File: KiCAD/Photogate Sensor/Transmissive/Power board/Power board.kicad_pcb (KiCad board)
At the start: 2 copper layers, 35 x 35 mm, 7 parts, among them J1 USB_B_Micro, J2 FFC Socket, J3 Conn_01x03_Socket, J4 DC Jack

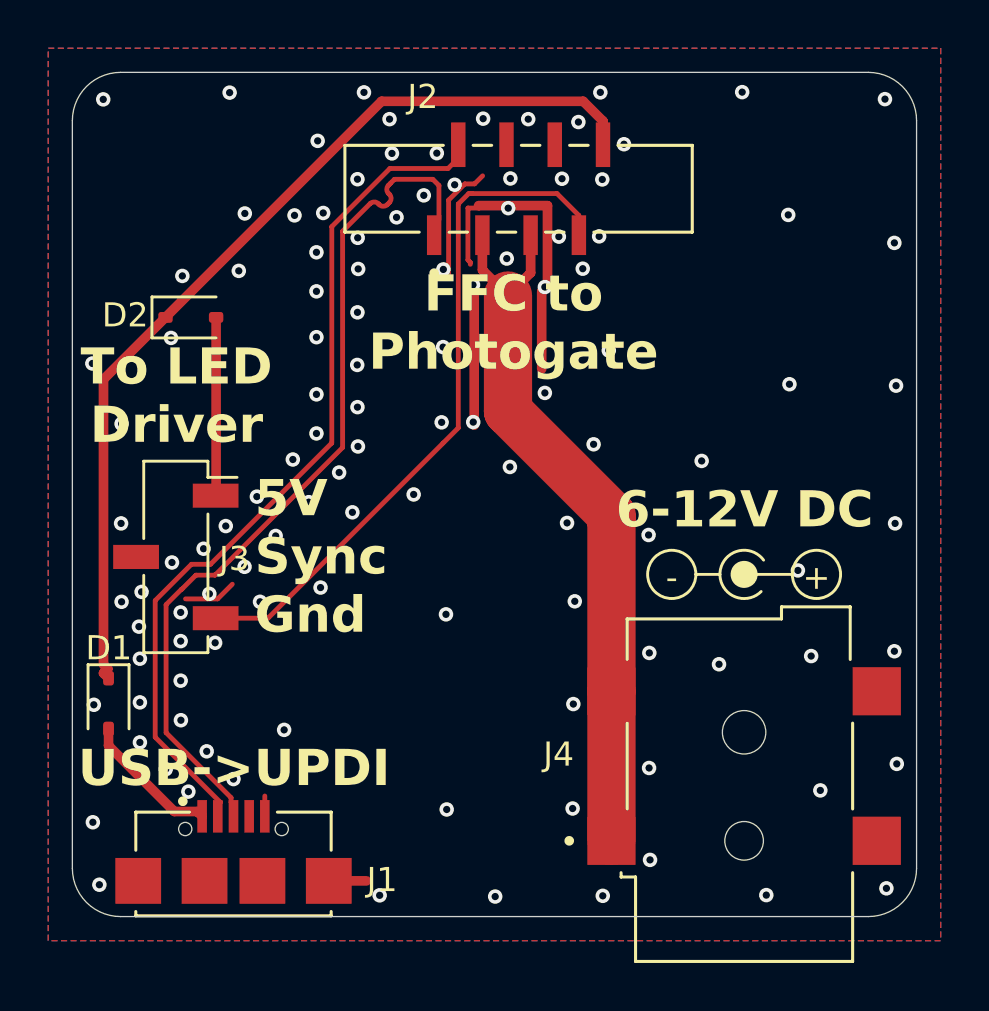
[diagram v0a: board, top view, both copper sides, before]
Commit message: USB skew matched and impedance set to approx. 90 ohms
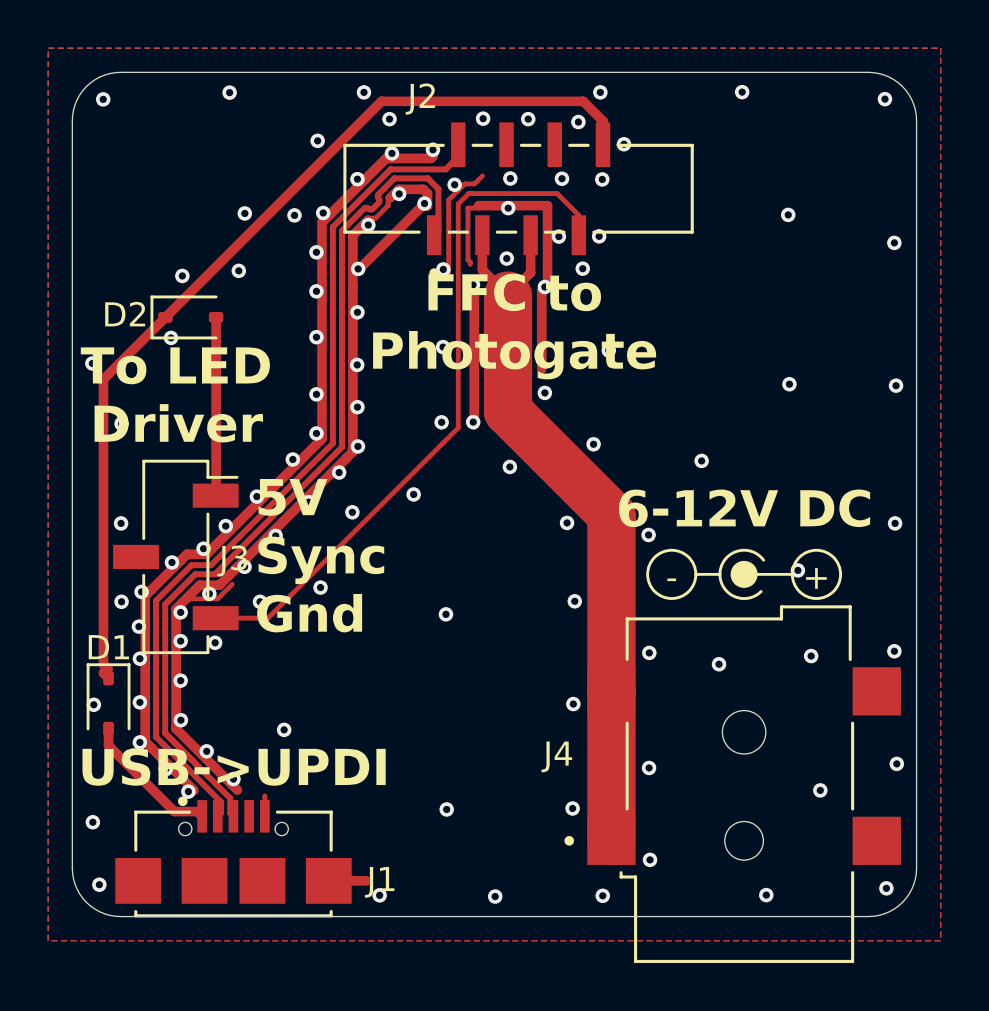
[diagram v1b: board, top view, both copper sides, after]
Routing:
- net GND: track 28.3 -> 98.7 mm
- net /D-: track 36.1 -> 37.6 mm
- net /D+: track 36.6 -> 37.8 mm

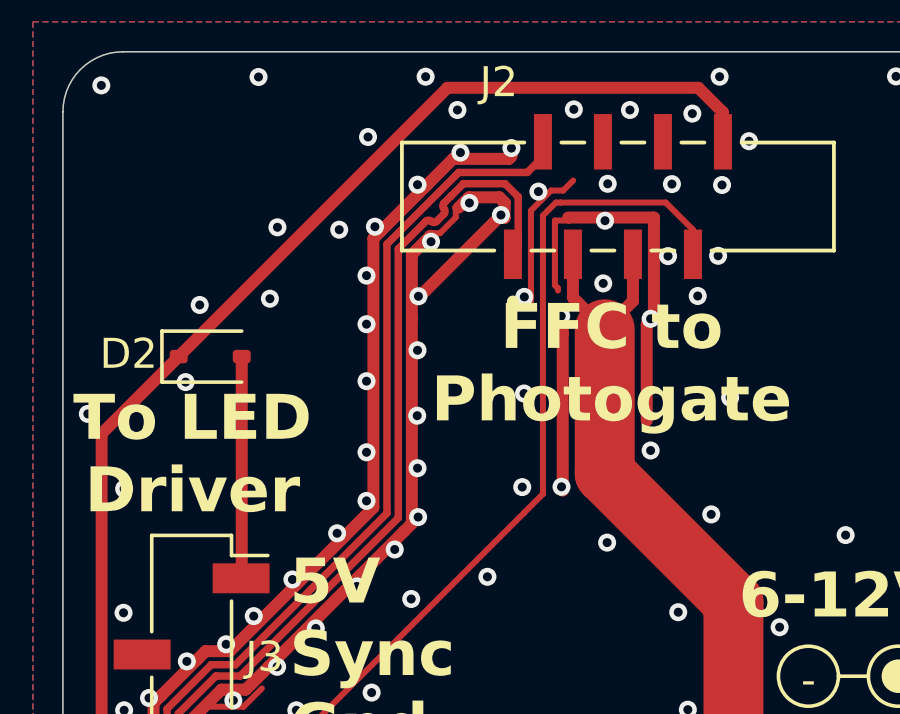
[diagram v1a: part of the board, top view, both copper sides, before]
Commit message: Add skew on power board D+ to offset skew on photogate board
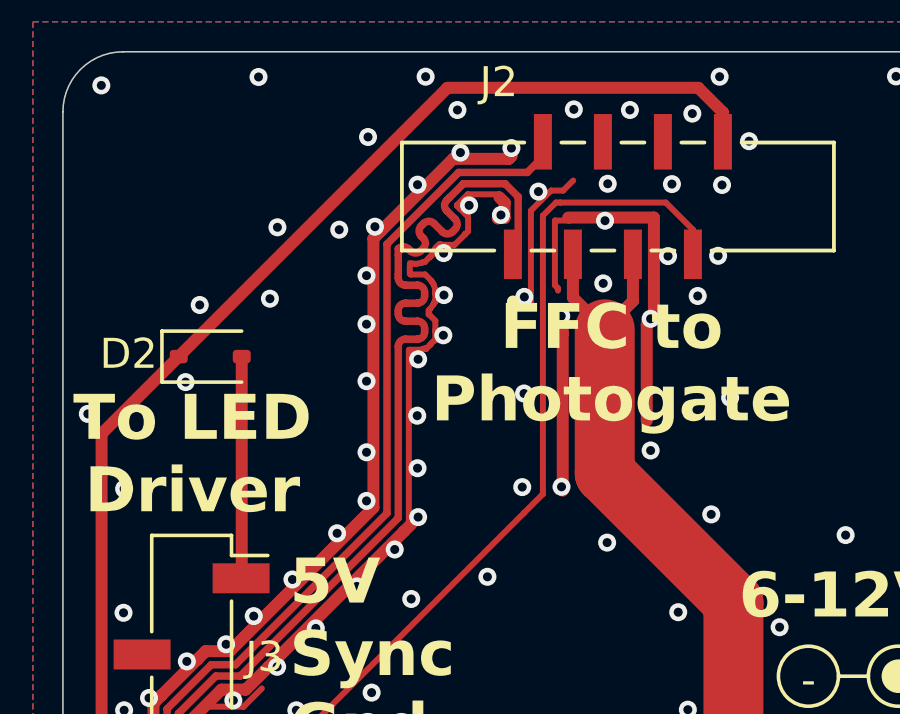
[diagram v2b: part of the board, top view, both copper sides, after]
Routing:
- net /D+: track 37.8 -> 42.2 mm
- net GND: track 98.7 -> 97.7 mm, vias 116 -> 117

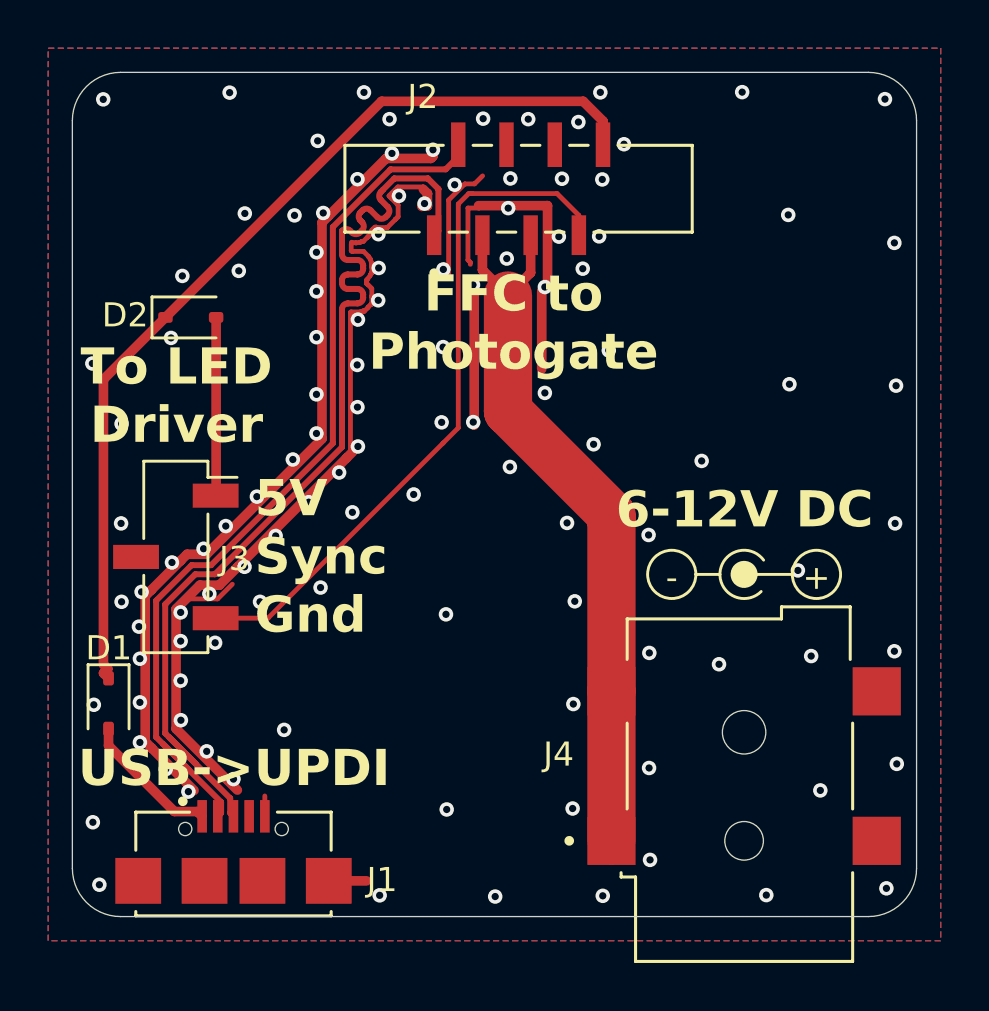
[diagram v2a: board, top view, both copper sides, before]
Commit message: Place Gnds closer to data lines on FFC
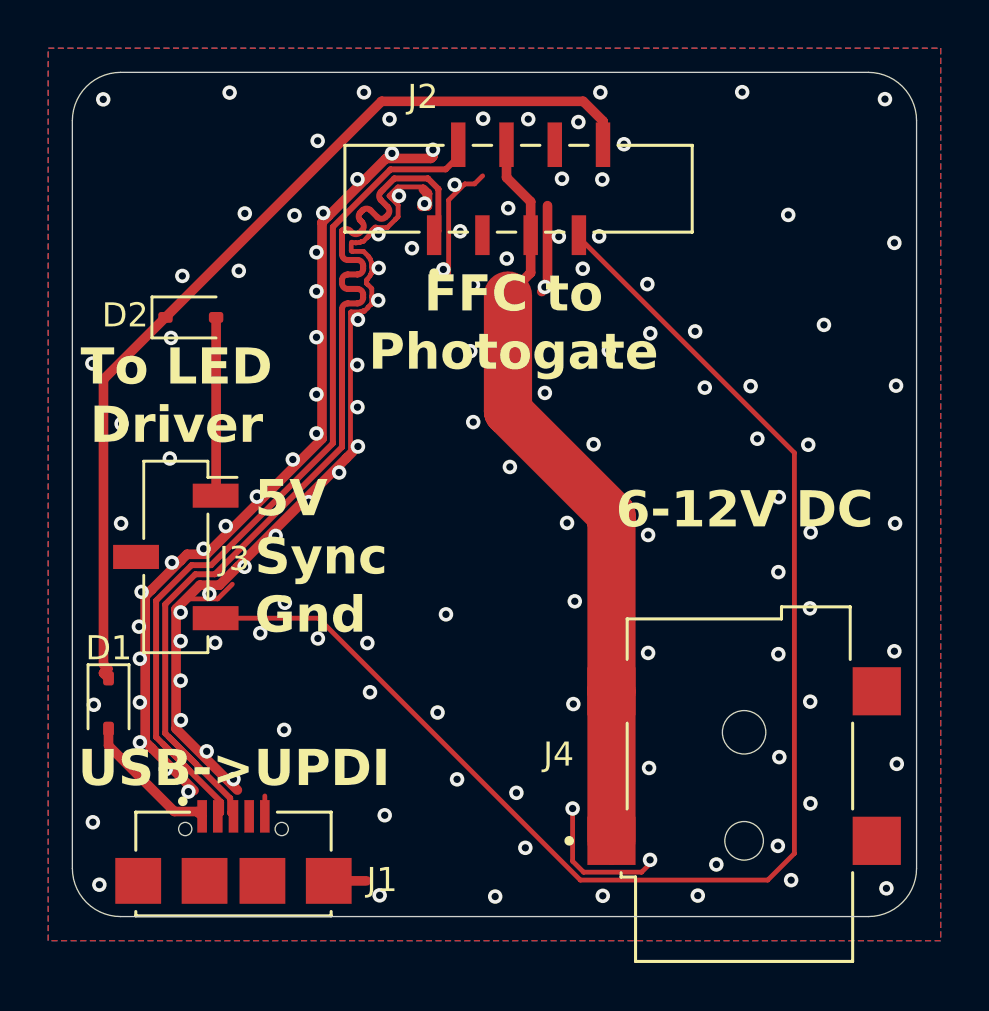
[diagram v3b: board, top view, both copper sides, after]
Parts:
- removed LOGO2: Jack Polarity, Custom Footprints:Polarity_Center_Positive
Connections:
- J2 pad 3: +12V -> GND
- J2 pad 4: GND -> +12V
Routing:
- net /Comp Out: track 29.0 -> 58.3 mm
- net GND: track 97.7 -> 88.6 mm, vias 117 -> 135
- net +12V: track 30.2 -> 31.4 mm

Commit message: More ground optimizations
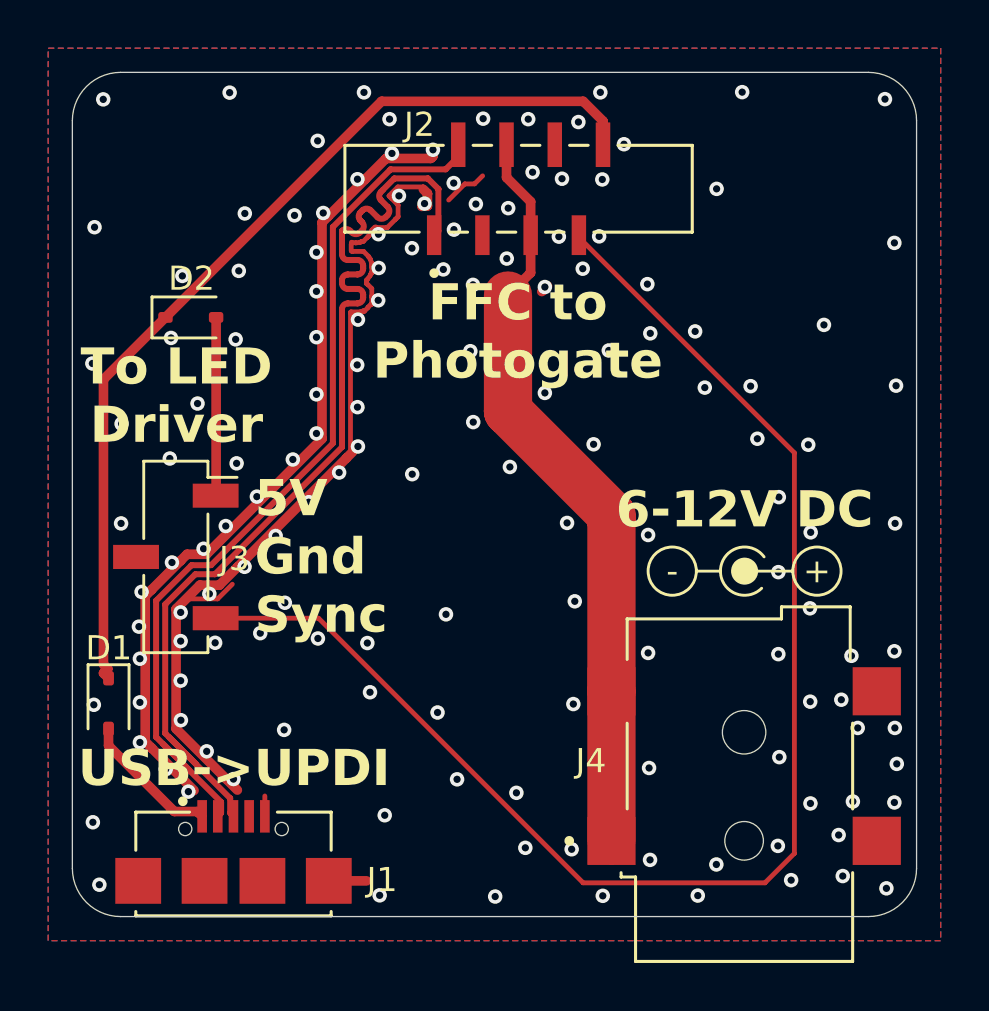
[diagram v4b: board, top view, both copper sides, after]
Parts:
- added SYM1: Logo_Open_Hardware_Small, Custom:polarity, F.Cu at (128.1, 119.3)
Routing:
- net GND: track 88.6 -> 76.3 mm, vias 135 -> 150
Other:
- board text added: "5V Gnd Sync"
- board text removed: "5V Sync Gnd"
